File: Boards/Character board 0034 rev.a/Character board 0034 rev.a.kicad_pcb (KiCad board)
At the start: 2 copper layers, 166.4 x 186.7 mm, 49 parts, among them J1 card edge, J2 character connector, Q1 2N6125, U1 2.2K, U10 Unused DIP, U11 ULN2003A, U12 ULN2003A, U13 7406, U2 2.2K, U3 Unused DIP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

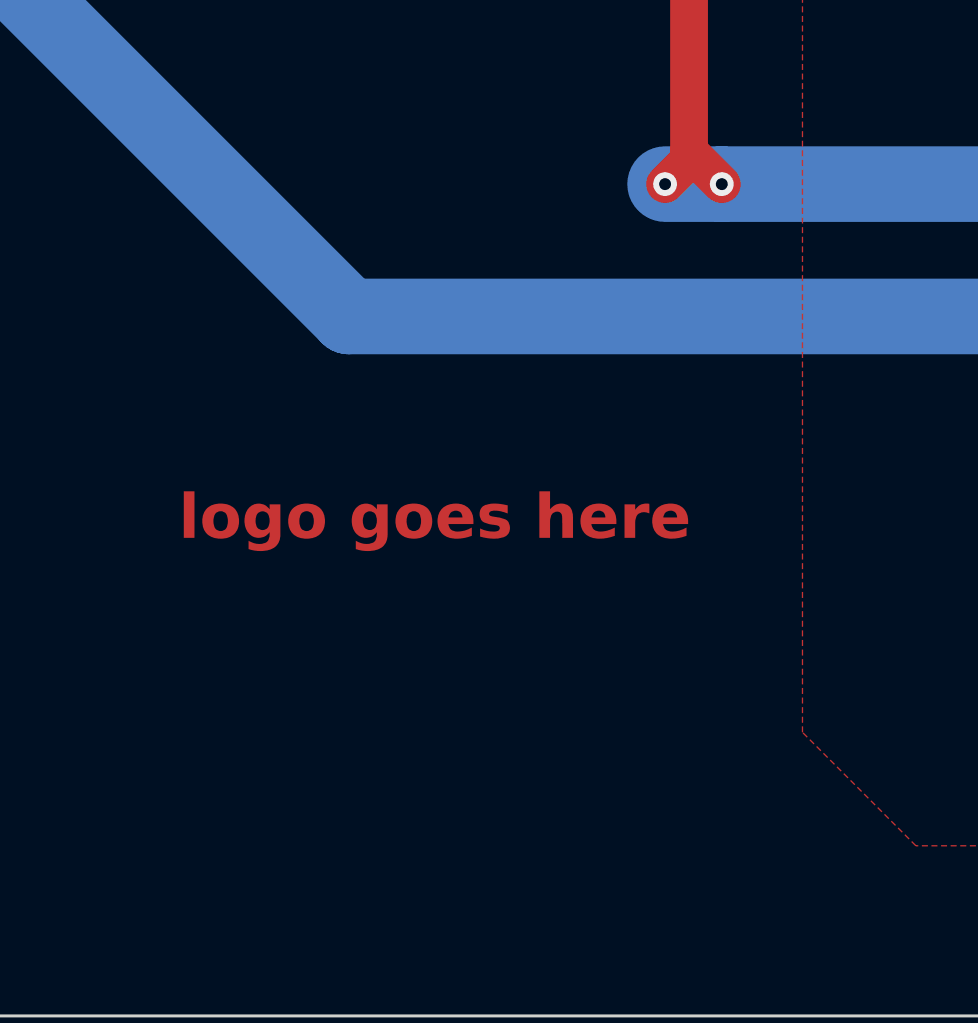
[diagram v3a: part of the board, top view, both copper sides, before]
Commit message: added logos
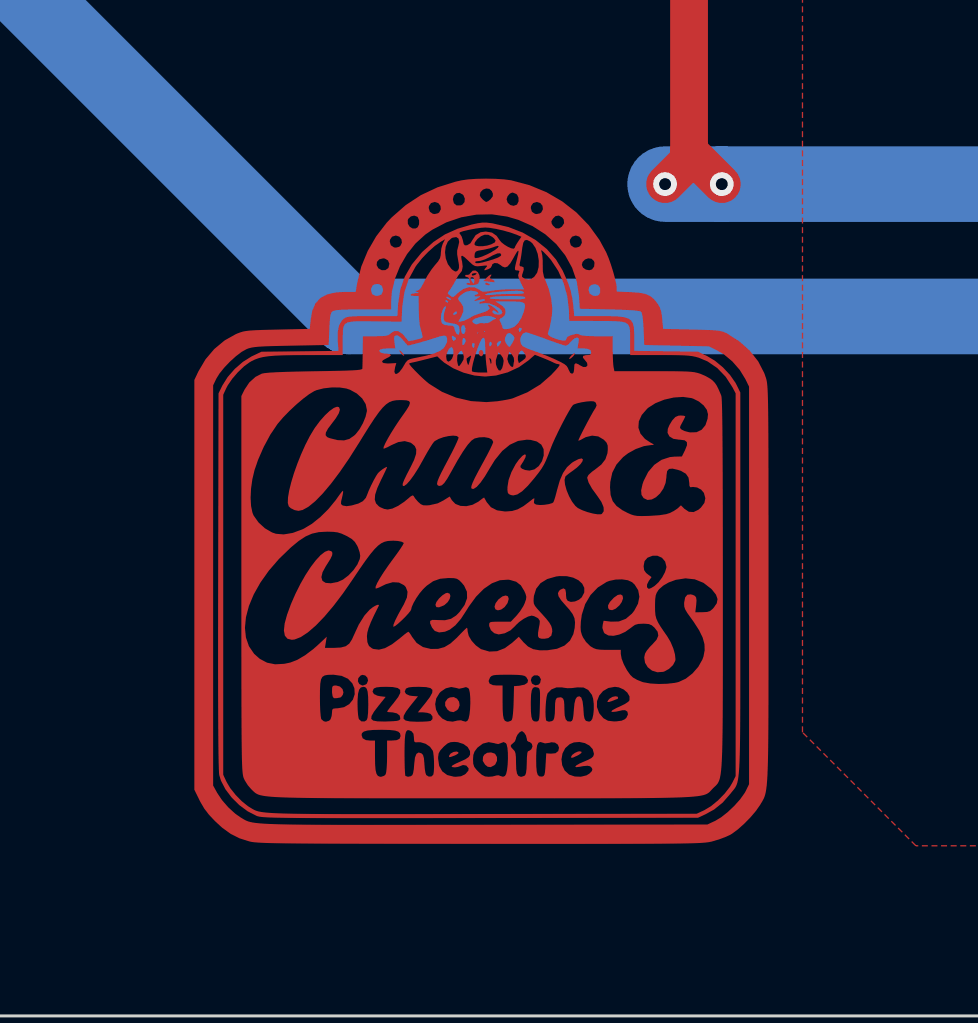
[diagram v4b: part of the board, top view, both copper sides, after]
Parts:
- added G***: LOGO, Evan's parts:ptt square, F.Cu at (53.3, 169.5)
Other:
- board text removed: "logo goes here"

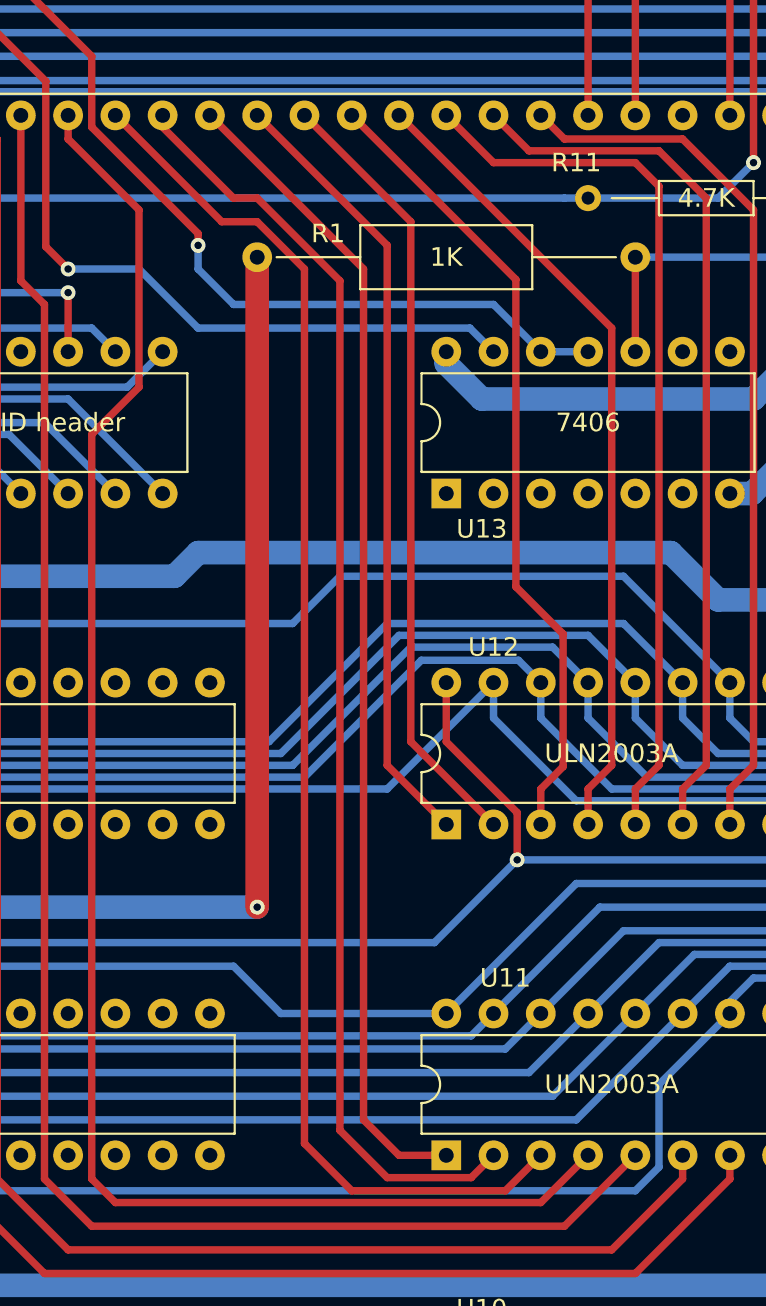
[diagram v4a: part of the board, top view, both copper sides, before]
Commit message: revisions from real life boards
tip130a is actually tip30a, widened holes for crystal, widened holes for big power resistor, fixed cpu board LED resistors
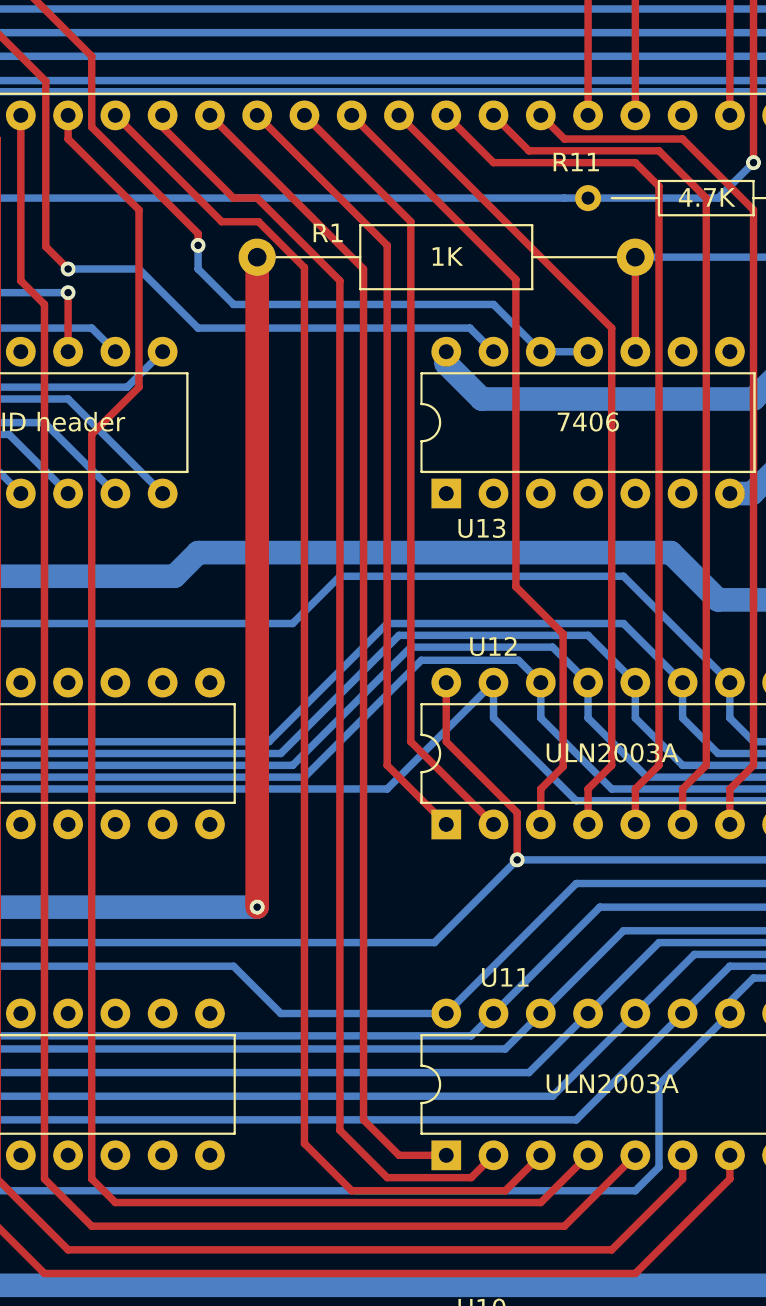
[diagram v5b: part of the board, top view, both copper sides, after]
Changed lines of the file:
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@@
     (fp_line (start 20.32 0) (end 14.66 0)
       (stroke (width 0.1) (type solid)) (layer "F.Fab"))
-    (pad "1" thru_hole circle (at 0 0) (size 1.6 1.6) (drill 0.8) (layers "*.Cu" "*.Mask")
+    (pad "1" thru_hole circle (at 0 0) (size 2 2) (drill 1) (layers "*.Cu" "*.Mask")
       (net 88 "Net-(Q1-B)") (pintype "passive"))
-    (pad "2" thru_hole oval (at 20.32 0) (size 1.6 1.6) (drill 0.8) (layers "*.Cu" "*.Mask")
+    (pad "2" thru_hole circle (at 20.32 0) (size 2 2) (drill 1) (layers "*.Cu" "*.Mask")
       (net 156 "Net-(C11-Pad1)") (pintype "passive"))
     (model "${KICAD6_3DMODEL_DIR}/Resistor_THT.3dshapes/R_Axial_DIN0309_L9.0mm_D3.2mm_P20.32mm_Horizontal.wrl"
@@
   (segment (start 120.65 103.505) (end 118.11 106.045) (width 0.4) (layer "F.Cu") (net 144))
   (segment (start 120.65 93.98) (end 120.65 103.505) (width 0.4) (layer "F.Cu") (net 144))
-  (segment (start 129.54 97.155) (end 129.54 144.145) (width 0.4) (layer "F.Cu") (net 145))
-  (segment (start 125.095 94.615) (end 127 94.615) (width 0.4) (layer "F.Cu") (net 145))
-  (segment (start 132.08 146.685) (end 140.335 146.685) (width 0.4) (layer "F.Cu") (net 145))
-  (segment (start 140.335 146.685) (end 142.24 144.78) (width 0.4) (layer "F.Cu") (net 145))
-  (segment (start 129.54 144.145) (end 132.08 146.685) (width 0.4) (layer "F.Cu") (net 145))
-  (segment (start 127 94.615) (end 129.54 97.155) (width 0.4) (layer "F.Cu") (net 145))
-  (segment (start 119.38 88.9) (end 125.095 94.615) (width 0.4) (layer "F.Cu") (net 145))
+  (segment (start 129.54 97.080101) (end 127.074899 94.615) (width 0.4) (layer "F.Cu") (net 145))
+  (segment (start 127.074899 94.615) (end 125.095 94.615) (width 0.4) (layer "F.Cu") (net 145))
+  (segment (start 142.24 144.78) (end 140.335 146.685) (width 0.4) (layer "F.Cu") (net 145))
+  (segment (start 129.54 144.145) (end 129.54 97.080101) (width 0.4) (layer "F.Cu") (net 145))
+  (segment (start 125.095 94.615) (end 119.38 88.9) (width 0.4) (layer "F.Cu") (net 145))
+  (segment (start 132.08 146.685) (end 129.54 144.145) (width 0.4) (layer "F.Cu") (net 145))
+  (segment (start 140.335 146.685) (end 132.08 146.685) (width 0.4) (layer "F.Cu") (net 145))
   (segment (start 127 93.345) (end 131.445 97.79) (width 0.4) (layer "F.Cu") (net 146))
   (segment (start 125.73 93.345) (end 127 93.345) (width 0.4) (layer "F.Cu") (net 146))

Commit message: added plans for 8216 substiturte board
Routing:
- net PB7: track 20.0 -> 0.00 mm
- net PB6: track 20.0 -> 0.00 mm
- net CB2: track 11.7 -> 0.00 mm
- net Net-(R13-Pad1): track 63.0 -> 58.8 mm
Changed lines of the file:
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@@
   (segment (start 138.43 100.33) (end 139.7 101.6) (width 0.4) (layer "B.Cu") (net 85))
   (segment (start 120.65 97.155) (end 123.825 100.33) (width 0.4) (layer "B.Cu") (net 85))
-  (segment (start 118.11 85.725) (end 118.11 89.535) (width 0.4) (layer "F.Cu") (net 86))
-  (segment (start 113.03 80.645) (end 118.11 75.565) (width 0.4) (layer "F.Cu") (net 86))
-  (segment (start 123.825 95.25) (end 123.825 95.885) (width 0.4) (layer "F.Cu") (net 86))
-  (segment (start 118.11 75.565) (end 118.11 63.5) (width 0.4) (layer "F.Cu") (net 86))
-  (segment (start 113.03 80.645) (end 118.11 85.725) (width 0.4) (layer "F.Cu") (net 86))
-  (segment (start 118.11 89.535) (end 123.825 95.25) (width 0.4) (layer "F.Cu") (net 86))
+  (segment (start 123.825 95.25) (end 118.11 89.535) (width 0.4) (layer "F.Cu") (net 86))
+  (segment (start 123.825 95.885) (end 123.825 95.25) (width 0.4) (layer "F.Cu") (net 86))
+  (segment (start 118.11 89.535) (end 118.11 63.5) (width 0.4) (layer "F.Cu") (net 86))
   (via (at 123.825 95.885) (size 0.8) (drill 0.4) (layers "F.Cu" "B.Cu") (net 86))
   (segment (start 123.825 95.885) (end 123.825 97.155) (width 0.4) (layer "B.Cu") (net 86))
@@
   (segment (start 46.355 58.42) (end 32.385 58.42) (width 0.4) (layer "F.Cu") (net 137))
   (segment (start 26.67 52.705) (end 24.13 52.705) (width 0.4) (layer "F.Cu") (net 137))
-  (segment (start 140.97 78.105) (end 140.97 70.485) (width 0.4) (layer "F.Cu") (net 138))
-  (segment (start 144.78 88.9) (end 144.78 81.915) (width 0.4) (layer "F.Cu") (net 138))
-  (segment (start 144.78 81.915) (end 140.97 78.105) (width 0.4) (layer "F.Cu") (net 138))
-  (segment (start 143.51 70.485) (end 143.51 78.105) (width 0.4) (layer "F.Cu") (net 139))
-  (segment (start 147.32 81.915) (end 147.32 88.9) (width 0.4) (layer "F.Cu") (net 139))
-  (segment (start 143.51 78.105) (end 147.32 81.915) (width 0.4) (layer "F.Cu") (net 139))
-  (segment (start 152.4 82.55) (end 152.4 88.9) (width 0.4) (layer "F.Cu") (net 140))
-  (segment (start 148.59 78.74) (end 152.4 82.55) (width 0.4) (layer "F.Cu") (net 140))
   (segment (start 147.32 151.13) (end 152.4 146.05) (width 0.4) (layer "F.Cu") (net 141))
   (segment (start 109.22 88.9) (end 110.49 90.17) (width 0.4) (layer "F.Cu") (net 141))
